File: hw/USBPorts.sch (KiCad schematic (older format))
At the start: 17 parts, among them J3 Conn_01x04, J4 USB_A, J5 Conn_01x04, J6 USB_A, J7 USB_A, J8 USB_A, U10 FSUSB31, U3 USB2517, U5 FSUSB31, U6 MIC2026-2BM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

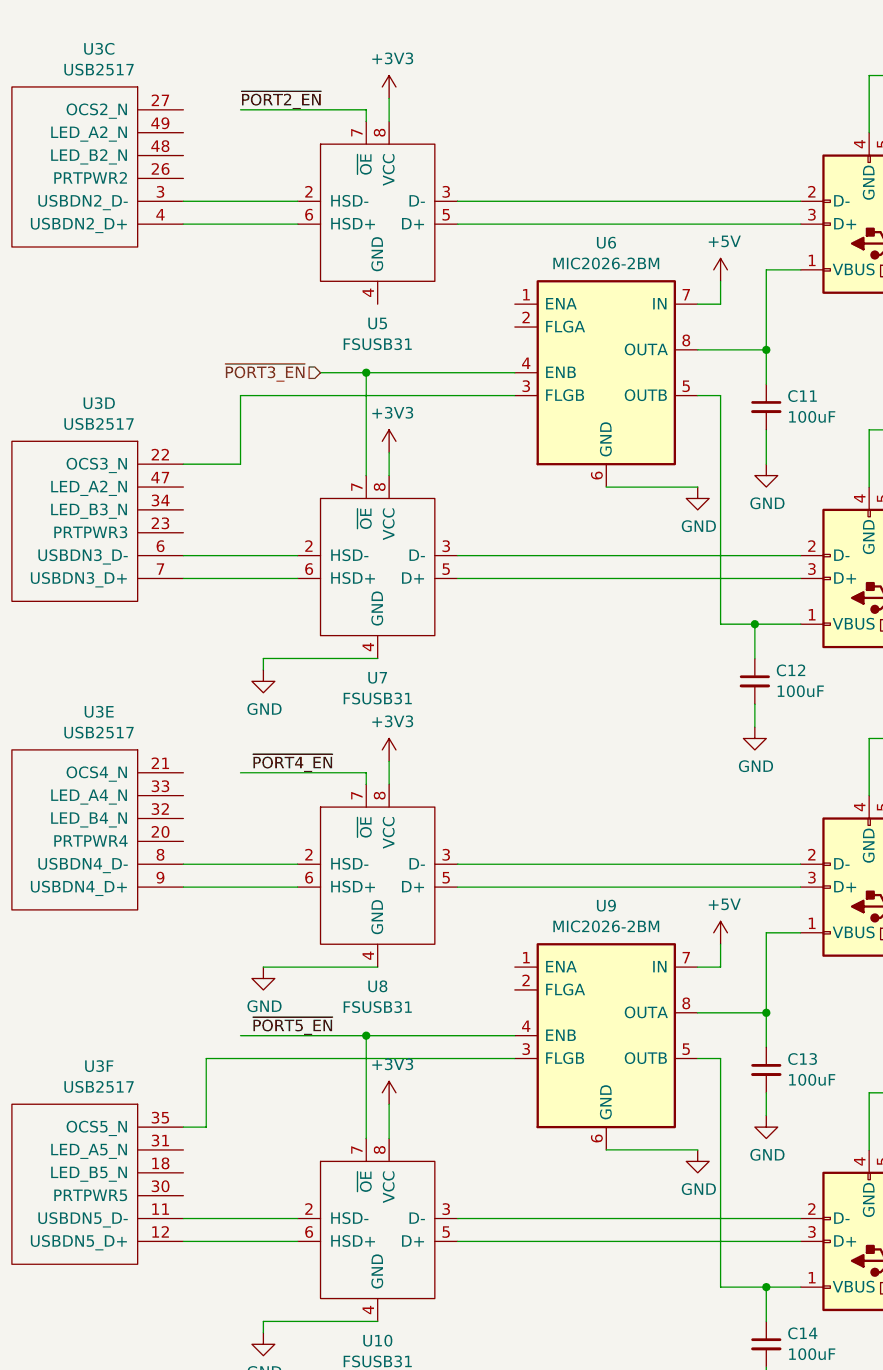
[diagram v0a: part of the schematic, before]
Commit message: Finish up usb port hookup
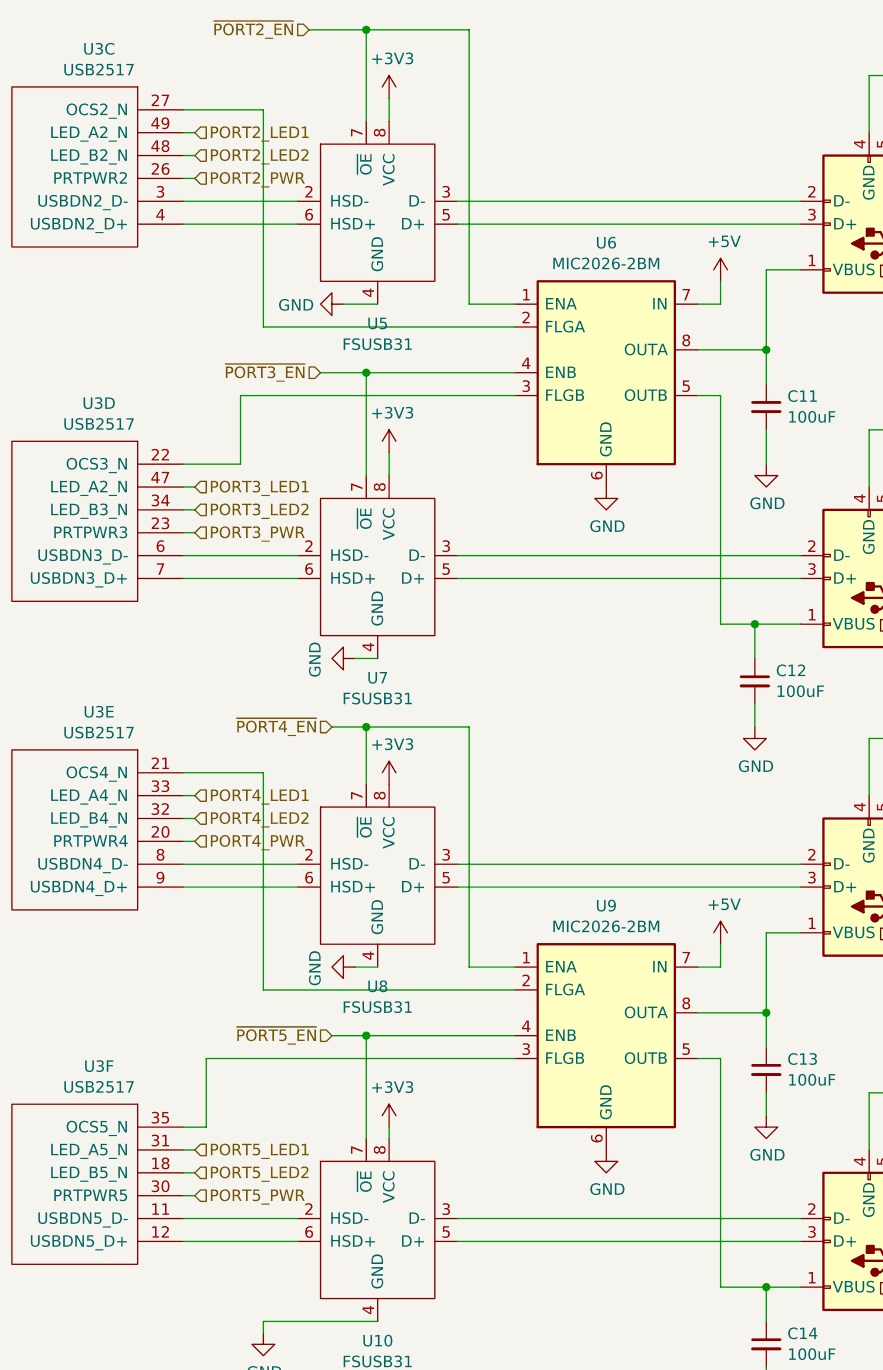
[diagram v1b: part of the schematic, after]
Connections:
- net GND: now also U5.4 (GND)
- net ~PORT2_EN~: now also U6.1 (ENA)
- net ~PORT4_EN~: now also U9.1 (ENA)
- net at U6.2 (FLGA): now also U3.27 (OCS2_N)
- net at U9.2 (FLGA): now also U3.21 (OCS4_N)
- net PORT2_PWR: now reaches U3.26 (PRTPWR2)
- net PORT2_LED2: now reaches U3.48 (LED_B2_N)
- net PORT2_LED1: now reaches U3.49 (LED_A2_N)
- net PORT3_PWR: now reaches U3.23 (PRTPWR3)
- net PORT3_LED2: now reaches U3.34 (LED_B3_N)
- net PORT3_LED1: now reaches U3.47 (LED_A2_N)
- net PORT4_PWR: now reaches U3.20 (PRTPWR4)
- net PORT4_LED2: now reaches U3.32 (LED_B4_N)
- net PORT4_LED1: now reaches U3.33 (LED_A4_N)
- net PORT5_LED2: now reaches U3.18 (LED_B5_N)
- net PORT5_PWR: now reaches U3.30 (PRTPWR5)
- net PORT5_LED1: now reaches U3.31 (LED_A5_N)
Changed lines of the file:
@@
 L power:+3V3 #PWR039
 U 1 1 5B95BD4A
-P 2800 4150
-F 0 "#PWR039" H 2800 4000 50  0001 C CNN
-F 1 "+3V3" H 2815 4323 50  0000 C CNN
-F 2 "" H 2800 4150 50  0001 C CNN
-F 3 "" H 2800 4150 50  0001 C CNN
-	1    2800 4150
+P 2800 4250
+F 0 "#PWR039" H 2800 4100 50  0001 C CNN
+F 1 "+3V3" H 2815 4423 50  0000 C CNN
+F 2 "" H 2800 4250 50  0001 C CNN
+F 3 "" H 2800 4250 50  0001 C CNN
+	1    2800 4250
 	1    0    0    -1
 $EndComp
@@
 L power:+3V3 #PWR043
 U 1 1 5B95BD6F
-P 2800 5650
-F 0 "#PWR043" H 2800 5500 50  0001 C CNN
-F 1 "+3V3" H 2815 5823 50  0000 C CNN
-F 2 "" H 2800 5650 50  0001 C CNN
-F 3 "" H 2800 5650 50  0001 C CNN
-	1    2800 5650
-	1    0    0    -1
-$EndComp
-Wire Wire Line
-	2800 5800 2800 5650
-Wire Wire Line
-	2800 4150 2800 4250
+P 2800 5750
+F 0 "#PWR043" H 2800 5600 50  0001 C CNN
+F 1 "+3V3" H 2815 5923 50  0000 C CNN
+F 2 "" H 2800 5750 50  0001 C CNN
+F 3 "" H 2800 5750 50  0001 C CNN
+	1    2800 5750
+	1    0    0    -1
+$EndComp
+Wire Wire Line
+	2800 5800 2800 5750
 Wire Wire Line
 	2800 2800 2800 2900
-Wire Wire Line
-	3750 2950 4150 2950
 $Comp
 L power:GND #PWR034
 U 1 1 5B95CE7A
-P 4150 2950
-F 0 "#PWR034" H 4150 2700 50  0001 C CNN
-F 1 "GND" H 4155 2777 50  0000 C CNN
-F 2 "" H 4150 2950 50  0001 C CNN
-F 3 "" H 4150 2950 50  0001 C CNN
-	1    4150 2950
+P 3750 2950
+F 0 "#PWR034" H 3750 2700 50  0001 C CNN
+F 1 "GND" H 3755 2777 50  0000 C CNN
+F 2 "" H 3750 2950 50  0001 C CNN
+F 3 "" H 3750 2950 50  0001 C CNN
+	1    3750 2950
 	1    0    0    -1
 $EndComp
@@
 Wire Wire Line
 	4600 4700 3100 4700
-Wire Wire Line
-	3750 5850 4150 5850
 $Comp
 L power:GND #PWR046
 U 1 1 5B95DC74
-P 4150 5850
-F 0 "#PWR046" H 4150 5600 50  0001 C CNN
-F 1 "GND" H 4155 5677 50  0000 C CNN
-F 2 "" H 4150 5850 50  0001 C CNN
-F 3 "" H 4150 5850 50  0001 C CNN
-	1    4150 5850
+P 3750 5850
+F 0 "#PWR046" H 3750 5600 50  0001 C CNN
+F 1 "GND" H 3755 5677 50  0000 C CNN
+F 2 "" H 3750 5850 50  0001 C CNN
+F 3 "" H 3750 5850 50  0001 C CNN
+	1    3750 5850
 	1    0    0    -1
 $EndComp
@@
 Wire Wire Line
 	5000 4050 4900 4050
-Text Label 2150 1300 0    50   ~ 0
-~PORT2_EN~
-Wire Wire Line
-	2700 1350 2700 1300
-Wire Wire Line
-	2700 1300 2150 1300
-Wire Wire Line
-	2700 4200 2150 4200
-Text Label 2200 4200 0    50   ~ 0
-~PORT4_EN~
-Wire Wire Line
-	2700 4250 2700 4200
-Wire Wire Line
-	2700 5350 2150 5350
-Text Label 2200 5350 0    50   ~ 0
-~PORT5_EN~
+Wire Wire Line
+	2700 4250 2700 4000
 Wire Wire Line
 	2700 5800 2700 5350
@@
 L power:GND #PWR037
 U 1 1 5B97B4AA
-P 2250 3750
-F 0 "#PWR037" H 2250 3500 50  0001 C CNN
-F 1 "GND" H 2255 3577 50  0000 C CNN
-F 2 "" H 2250 3750 50  0001 C CNN
-F 3 "" H 2250 3750 50  0001 C CNN
-	1    2250 3750
-	1    0    0    -1
-$EndComp
-Wire Wire Line
-	2750 3700 2250 3700
-Wire Wire Line
-	2250 3700 2250 3750
+P 2650 3700
+F 0 "#PWR037" H 2650 3450 50  0001 C CNN
+F 1 "GND" H 2655 3527 50  0000 C CNN
+F 2 "" H 2650 3700 50  0001 C CNN
+F 3 "" H 2650 3700 50  0001 C CNN
+	1    2650 3700
+	0    1    1    0
+$EndComp
+Wire Wire Line
+	2750 3700 2650 3700
 $Comp
 L power:GND #PWR042
 U 1 1 5B97CF4D
-P 2250 5050
-F 0 "#PWR042" H 2250 4800 50  0001 C CNN
-F 1 "GND" H 2255 4877 50  0000 C CNN
-F 2 "" H 2250 5050 50  0001 C CNN
-F 3 "" H 2250 5050 50  0001 C CNN
-	1    2250 5050
-	1    0    0    -1
-$EndComp
-Wire Wire Line
-	2750 5050 2250 5050
+P 2650 5050
+F 0 "#PWR042" H 2650 4800 50  0001 C CNN
+F 1 "GND" H 2655 4877 50  0000 C CNN
+F 2 "" H 2650 5050 50  0001 C CNN
+F 3 "" H 2650 5050 50  0001 C CNN
+	1    2650 5050
+	0    1    1    0
+$EndComp
+Wire Wire Line
+	2750 5050 2650 5050
 $Comp
 L power:GND #PWR047
@@
 Wire Wire Line
 	3350 5350 2700 5350
+Wire Wire Line
+	2700 4000 3150 4000
+Wire Wire Line
+	3150 4000 3150 5050
+Wire Wire Line
+	3150 5050 3350 5050
+Text HLabel 2450 950  0    50   Input ~ 0
+~PORT2_EN~
+Wire Wire Line
+	2450 950  2700 950
+Wire Wire Line
+	2700 950  2700 1350
+Wire Wire Line
+	2700 950  3150 950
+Wire Wire Line
+	3150 950  3150 2150
+Wire Wire Line
+	3150 2150 3350 2150
+Connection ~ 2700 950
+$Comp
+L power:GND #PWR?
+U 1 1 5BA4A335
+P 2600 2150
+F 0 "#PWR?" H 2600 1900 50  0001 C CNN
+F 1 "GND" V 2605 2022 50  0000 R CNN
+F 2 "" H 2600 2150 50  0001 C CNN
+F 3 "" H 2600 2150 50  0001 C CNN
+	1    2600 2150
+	0    1    1    0
+$EndComp
+Wire Wire Line
+	2750 2150 2600 2150
+Wire Wire Line
+	3350 2250 2250 2250
+Wire Wire Line
+	2250 2250 2250 1300
+Wire Wire Line
+	2250 1300 1900 1300
+Text HLabel 1950 1400 2    50   Input ~ 0
+PORT2_LED1
+Text HLabel 1950 1500 2    50   Input ~ 0
+PORT2_LED2
+Wire Wire Line
+	1950 1500 1900 1500
+Wire Wire Line
+	1950 1400 1900 1400
+Text HLabel 1950 1600 2    50   Input ~ 0
+PORT2_PWR
+Wire Wire Line
+	1950 1600 1900 1600
+Text HLabel 1950 2950 2    50   Input ~ 0
+PORT3_LED1
+Text HLabel 1950 3050 2    50   Input ~ 0
+PORT3_LED2
+Wire Wire Line
+	1950 3050 1900 3050
+Wire Wire Line
+	1950 2950 1900 2950
+Text HLabel 1950 3150 2    50   Input ~ 0
+PORT3_PWR
+Wire Wire Line
+	1950 3150 1900 3150
+Text HLabel 1950 4300 2    50   Input ~ 0
+PORT4_LED1
+Text HLabel 1950 4400 2    50   Input ~ 0
+PORT4_LED2
+Wire Wire Line
+	1950 4400 1900 4400
+Wire Wire Line
+	1950 4300 1900 4300
+Text HLabel 1950 4500 2    50   Input ~ 0
+PORT4_PWR
+Wire Wire Line
+	1950 4500 1900 4500
+Text HLabel 1950 5850 2    50   Input ~ 0
+PORT5_LED1
+Text HLabel 1950 5950 2    50   Input ~ 0
+PORT5_LED2
+Wire Wire Line
+	1950 5950 1900 5950
+Wire Wire Line
+	1950 5850 1900 5850
+Text HLabel 1950 6050 2    50   Input ~ 0
+PORT5_PWR
+Wire Wire Line
+	1950 6050 1900 6050
+Text HLabel 2550 4000 0    50   Input ~ 0
+~PORT4_EN~
+Wire Wire Line
+	2700 4000 2550 4000
+Wire Wire Line
+	3350 5150 2250 5150
+Wire Wire Line
+	2250 5150 2250 4200
+Wire Wire Line
+	2250 4200 1900 4200
+Connection ~ 2700 4000
+Text HLabel 2550 5350 0    50   Input ~ 0
+~PORT5_EN~
+Wire Wire Line
+	2700 5350 2550 5350
 Connection ~ 2700 5350
 $EndSCHEMATC
